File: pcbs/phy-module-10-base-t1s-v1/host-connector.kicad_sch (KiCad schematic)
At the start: 1 part, among them J501 PHY Interface V2 Plug

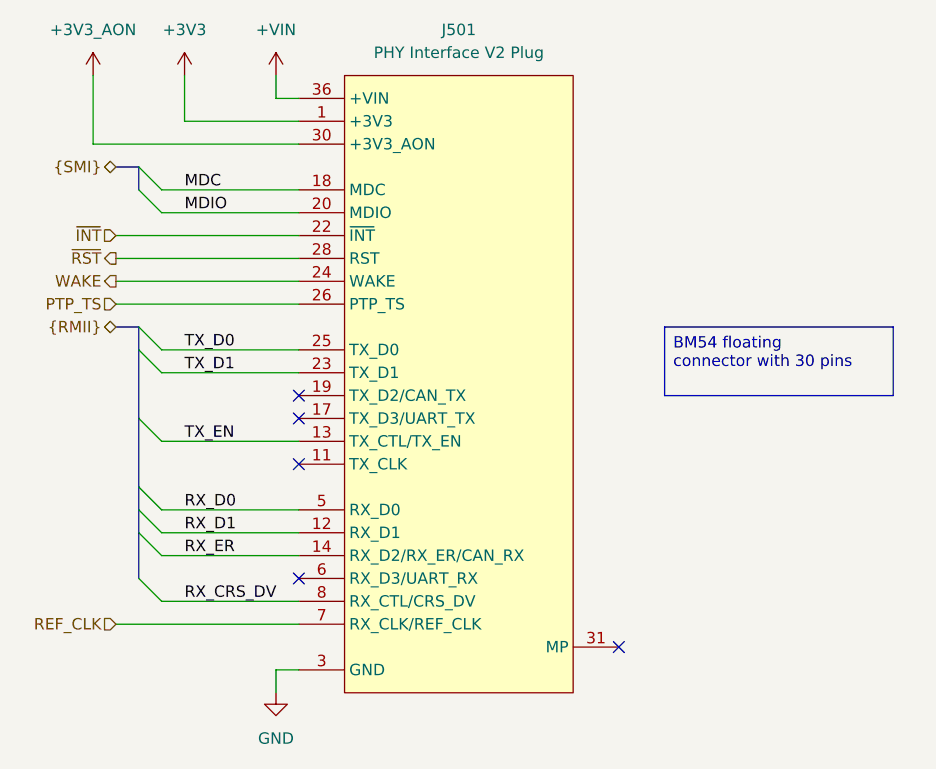
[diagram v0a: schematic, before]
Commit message: [10base-t1s] Updated schematic symbols
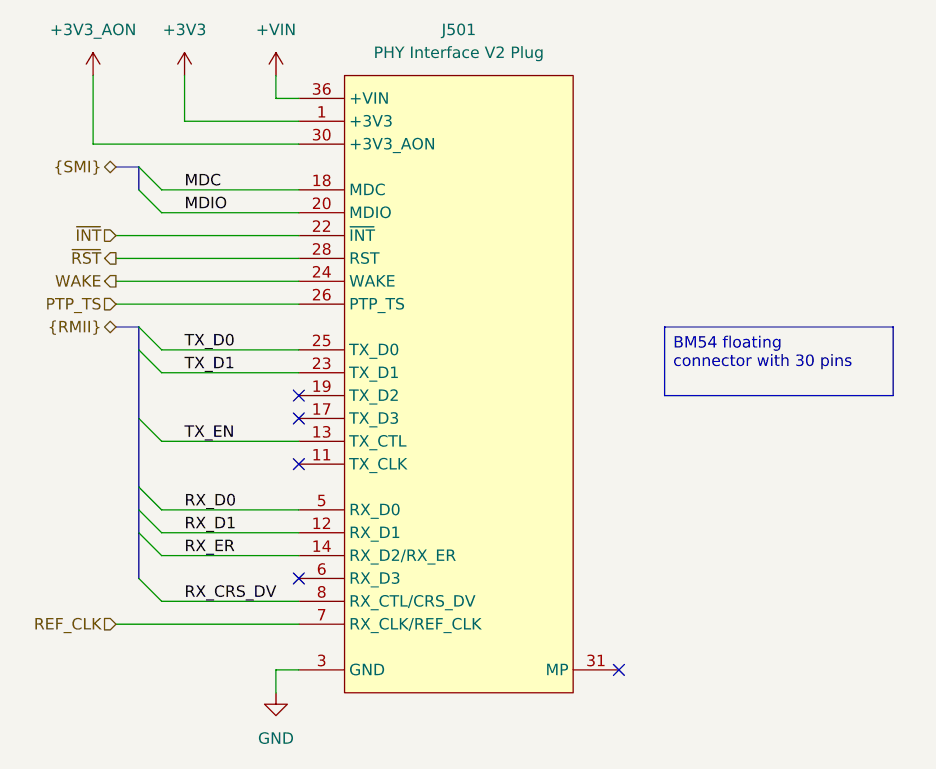
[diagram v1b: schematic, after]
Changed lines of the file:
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@@
 	)
 	(no_connect
-		(at 175.26 127)
+		(at 175.26 129.54)
 	)
 	(no_connect
